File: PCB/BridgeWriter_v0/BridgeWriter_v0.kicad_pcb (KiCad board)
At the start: 4 copper layers, 100 x 60 mm, 195 parts, among them J1 USB_B, J10 Conn_01x04, J17 Conn_01x01, J18 Conn_01x01, J2 RJ45_Bel_SI-60062-F, J24 Conn_01x04, J25 Conn_01x04, J3 Conn_01x05, J4 Conn_01x06, J6 Conn_01x04, J7 Conn_01x04, J9 Micro_SD_Card_Det2, SW1 SW_Push, SW10 SW_Push, SW2 BOOT_MODE0, SW3 SW_Push, SW4 SW_Push, SW5 SW_Push, SW6 SW_Push, SW7 SW_Push, SW8 BOOT_MODE1, SW9 SW_Push, U1 STM32H723VGTx, U10 ADP3338AKCZ-3.3, U11 OKL-T/6-W12N-C, U2 W6300, U3 ESP32-C5-WROOM-1, U5 MCP2562-E-SN, U6 MCP2562-E-SN, U7 USB3343, U8 ADP3338AKCZ-3.3, U9 CH213K, Y1 FC2012SN 32.768K-70NNA0KC0, Y2 XRCGB25M000FFS1AR0, Y3 ECS-600-8-36B-CTN-TR

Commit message: change
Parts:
- removed C25, C26: 0.1uF, Capacitor_SMD:C_0603_1608Metric_Pad1.08x0.95mm_HandSolder
- removed J10: Conn_01x04, Connector_PinSocket_2.54mm:PinSocket_1x04_P2.54mm_Vertical
- added U12: PT86-091940LMR, My_Library:PT86-091940LMR, F.Cu at (189.6, 77.7)
- added U4: TLP293, Package_SO:SOIC-4_4.55x2.6mm_P1.27mm, B.Cu at (208.2, 127.0)
- C10, C3, C35, C49, C6, C61, R19, R20, R21, R22, R23, R25, R47, U6: moved to B.Cu
- R55: value 80k -> 10k; moved to B.Cu
- R56: value 10k -> 1k; moved to B.Cu
- moved C35 126.6 mm to (230.7, 92.1)
- moved C61 121.9 mm to (226.9, 92.2)
- moved R25 117.3 mm to (230.7, 90.7), turned to 180 degrees
- moved SW8 112.2 mm to (186.3, 124.2), turned to 90 degrees
- moved SW2 105.5 mm to (177.9, 124.3), turned to 90 degrees
- moved R47 105.4 mm to (226.9, 90.7), turned to 180 degrees
- moved R55 95.7 mm to (213.2, 127.3), turned to 90 degrees
- moved R56 85.0 mm to (202.2, 128.7), turned to 180 degrees
- moved R2 79.9 mm to (182.0, 120.9)
- moved C31 60.3 mm to (201.0, 109.2), turned to 180 degrees
- moved C51 55.6 mm to (188.1, 106.3), turned to -135 degrees
- moved C33 55.0 mm to (187.2, 104.5), turned to -90 degrees
- moved R23 53.5 mm to (142.4, 122.1), turned to 90 degrees
- moved C34 53.3 mm to (201.0, 108.0), turned to 180 degrees
- moved R19 51.6 mm to (154.4, 122.1), turned to 90 degrees
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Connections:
- J3 pad 2: SWDIO -> SWCLK
- J3 pad 3: SWCLK -> SWDIO
- J3 pad 4: +3.3V -> GND
- J3 pad 5: GND -> +3.3V
- R55 pad 2: POWER_MONITOR -> Net-(R55-Pad2)
- R56 pad 1: POWER_MONITOR -> Net-(R56-Pad1)
- R56 pad 2: GND -> +3.3V
- U1 pad 68: LPUART_TXD -> unconnected-(U1-PA9-Pad68)
- U1 pad 69: LPUART_RXD -> unconnected-(U1-PA10-Pad69)
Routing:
- net NRST: track 0.00 -> 43.7 mm, vias 0 -> 2
- net +3.3V: track 55.5 -> 83.4 mm, vias 7 -> 9
- net ESP_3.3V: track 16.7 -> 27.0 mm, vias 0 -> 1
- net SWDIO: track 0.00 -> 9.88 mm
- net SWCLK: track 0.00 -> 9.40 mm
- net Net-(R56-Pad1): track 0.00 -> 6.59 mm
- net Net-(C30-Pad1): track 0.00 -> 3.10 mm
- net Net-(C31-Pad1): track 0.00 -> 2.95 mm
- net Net-(R55-Pad2): track 0.00 -> 1.78 mm
- net ESP32_EN: track 0.00 -> 1.46 mm, vias 0 -> 1
- net ESP32_IO0: track 0.00 -> 1.45 mm, vias 0 -> 1
- net Wi-Fi_RESET: track 0.00 -> 0.66 mm, vias 0 -> 1
- net USB_RESET: track 0.00 -> 0.66 mm, vias 0 -> 1
- net FDCAN2_RESET: track 0.00 -> 0.66 mm, vias 0 -> 1
- net FDCAN1_RESET: track 0.00 -> 0.66 mm, vias 0 -> 1
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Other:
- board text added: "Ethernet"
- board text added: "FDCAN1"
- board text added: "FDCAN2"
- board text added: "GND"
- board text added: "MAX 14V"
- board text added: "RESET"
- board text added: "USB"
- board text added: "VCC"
- board text added: "Wi-Fi"

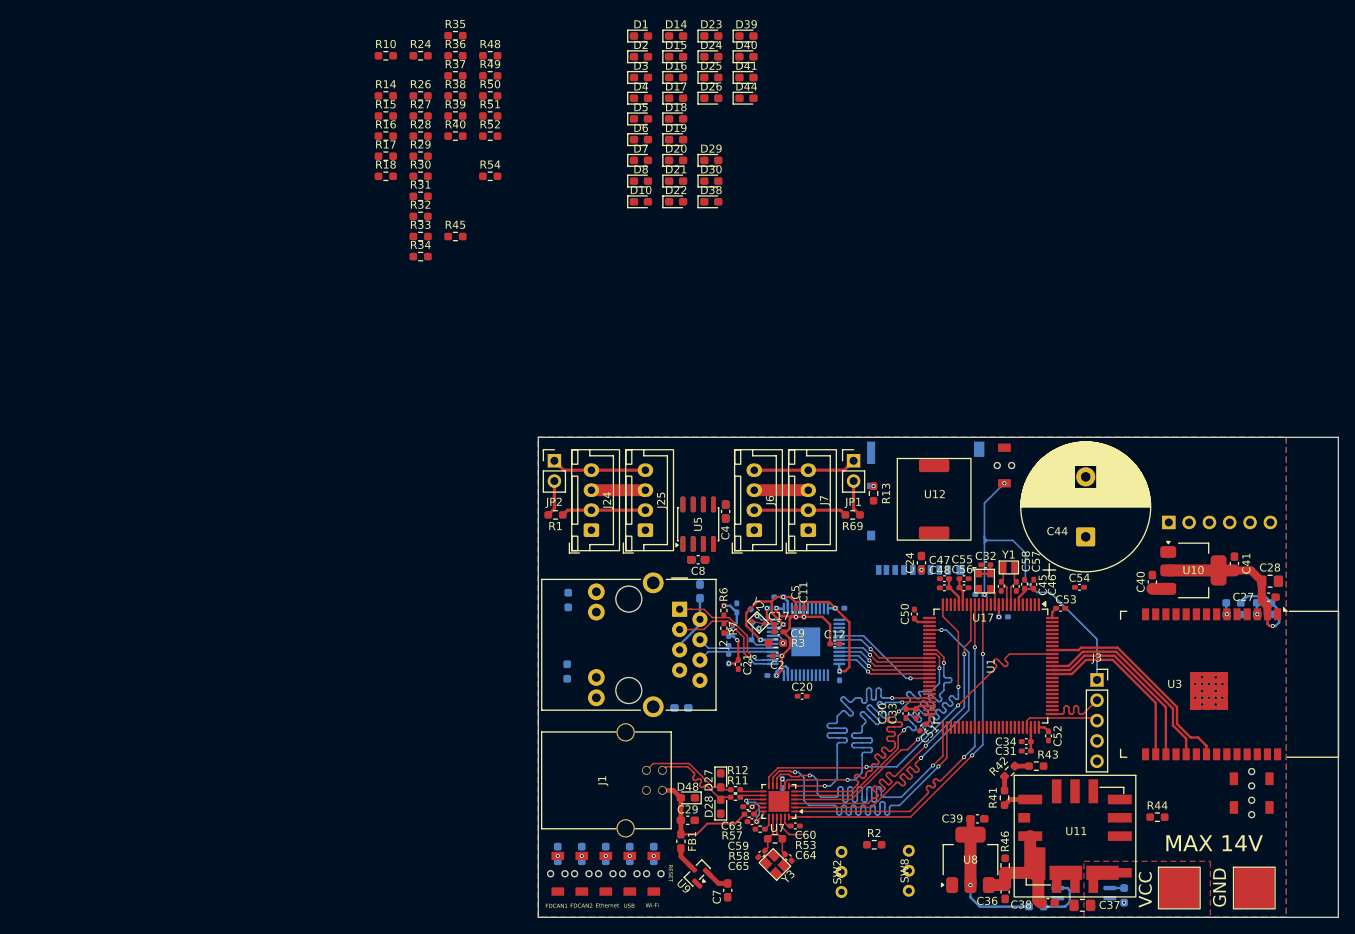
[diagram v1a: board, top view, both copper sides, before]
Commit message: All the wiring except the power is probably done.
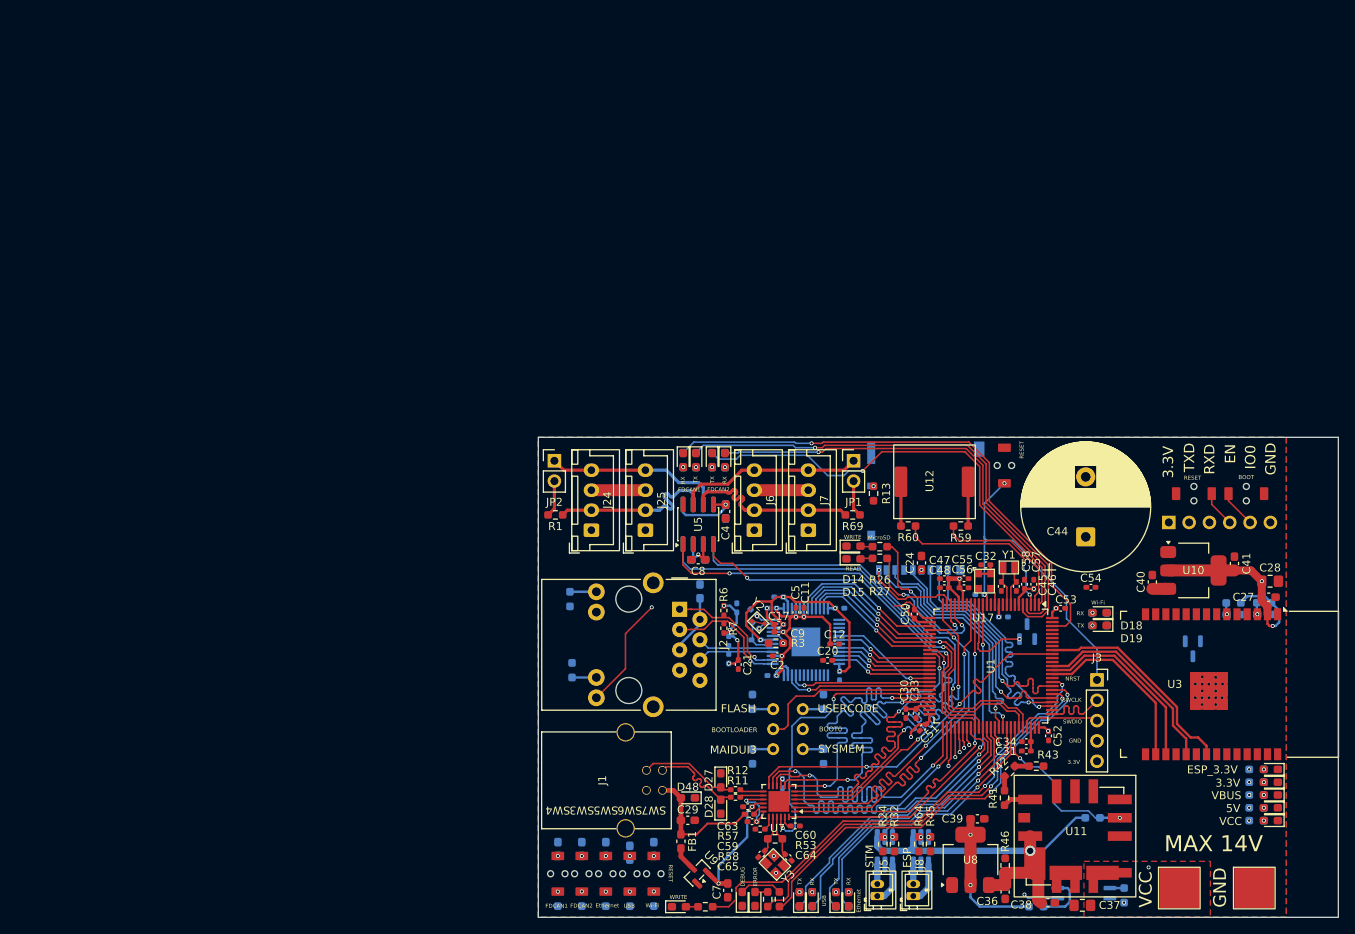
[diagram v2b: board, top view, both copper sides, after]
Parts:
- removed C1: 1uF, Capacitor_SMD:C_0603_1608Metric_Pad1.08x0.95mm_HandSolder
- removed D16, D38, D39: O, LED_SMD:LED_0603_1608Metric_Pad1.05x0.95mm_HandSolder
- removed D17, D20, D7: G, LED_SMD:LED_0603_1608Metric_Pad1.05x0.95mm_HandSolder
- removed D4, D8: W, LED_SMD:LED_0603_1608Metric_Pad1.05x0.95mm_HandSolder
- removed D44: LED, LED_SMD:LED_0603_1608Metric_Pad1.05x0.95mm_HandSolder
- removed R16, R28, R29, R48, R49, R52: 1k, Resistor_SMD:R_0603_1608Metric_Pad0.98x0.95mm_HandSolder
- added C25: 0.1uF, Capacitor_SMD:C_0603_1608Metric_Pad1.08x0.95mm_HandSolder, B.Cu at (154.4, 121.5)
- added C26: 0.1uF, Capacitor_SMD:C_0603_1608Metric_Pad1.08x0.95mm_HandSolder, B.Cu at (151.4, 121.9)
- added C66: 0.1uF, Capacitor_SMD:C_0603_1608Metric_Pad1.08x0.95mm_HandSolder, B.Cu at (142.4, 121.5)
- added C67: 0.1uF, Capacitor_SMD:C_0603_1608Metric_Pad1.08x0.95mm_HandSolder, B.Cu at (145.4, 121.5)
- added C68: 0.1uF, Capacitor_SMD:C_0603_1608Metric_Pad1.08x0.95mm_HandSolder, B.Cu at (148.4, 121.5)
- added J5: Conn_01x02, Connector_JST:JST_ZH_B2B-ZR_1x02_P1.50mm_Vertical, F.Cu at (182.4, 127.3)
- added J8: Conn_01x02, Connector_JST:JST_ZH_B2B-ZR_1x02_P1.50mm_Vertical, F.Cu at (186.9, 127.3)
- added R59: 330, Resistor_SMD:R_0603_1608Metric_Pad0.98x0.95mm_HandSolder, F.Cu at (192.8, 81.1)
- added R60: 330, Resistor_SMD:R_0603_1608Metric_Pad0.98x0.95mm_HandSolder, F.Cu at (186.2, 81.1)
- added R61: 1k, Resistor_SMD:R_0603_1608Metric_Pad0.98x0.95mm_HandSolder, B.Cu at (154.4, 127.7)
- added R62: 1k, Resistor_SMD:R_0603_1608Metric_Pad0.98x0.95mm_HandSolder, B.Cu at (166.8, 109.9)
- added R63: 10k, Resistor_SMD:R_0603_1608Metric_Pad0.98x0.95mm_HandSolder, B.Cu at (166.8, 103.1)
- added R64: 1k, Resistor_SMD:R_0603_1608Metric_Pad0.98x0.95mm_HandSolder, F.Cu at (187.6, 120.8)
- added U13: AM8068, Package_TO_SOT_SMD:TSOT-23-6_HandSoldering, B.Cu at (183.3, 121.7)
- added U14: AM8068, Package_TO_SOT_SMD:TSOT-23-6_HandSoldering, B.Cu at (187.8, 121.7)
- added U15: MCP9700x-ETT, Package_TO_SOT_SMD:SOT-23, B.Cu at (221.8, 96.4)
- added U16: MCP9700x-ETT, Package_TO_SOT_SMD:SOT-23, B.Cu at (201.1, 94.3)
- D15, D19, D22, D24, D26, D30: value B -> G
- R10, R14, R15, R17, R2, R30, R31, R33, R34, R35, R36, R37, R38, R39, R40, R44, R54: moved to B.Cu
- moved R10 142.8 mm to (229.8, 114.7)
- moved R14 141.6 mm to (229.8, 117.9)
- moved R15 139.0 mm to (229.8, 116.3)
- moved R17 134.0 mm to (229.8, 113.1)
- moved D1 125.8 mm to (231.6, 117.9), turned to 180 degrees
- moved D2 122.5 mm to (231.6, 116.3), turned to 180 degrees
- moved R54 121.1 mm to (229.8, 111.5)
- moved D3 119.3 mm to (231.6, 114.7), turned to 180 degrees
- moved D5 114.3 mm to (231.6, 113.1), turned to 180 degrees
- moved R24 114.2 mm to (183.1, 120.9), turned to -90 degrees
- moved R39 108.8 mm to (177.2, 127.7), turned to 90 degrees
- moved R40 107.3 mm to (178.8, 127.7), turned to 90 degrees
- moved R50 106.7 mm to (170.1, 127.7), turned to 90 degrees
- moved D10 106.0 mm to (231.6, 111.5), turned to 180 degrees
- moved D40 105.3 mm to (165.5, 127.7), turned to 90 degrees
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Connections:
- J2 pad SH: Net-(C1-Pad1) -> unconnected-(J2-PadSH)_1
- R19 pad 1: Wi-Fi_RESET -> +3.3V
- R19 pad 2: GND -> Net-(R19-Pad2)
- R20 pad 1: USB_RESET -> +3.3V
- R20 pad 2: GND -> Net-(R20-Pad2)
- R21 pad 1: Ethernet_RESET -> +3.3V
- R21 pad 2: GND -> Net-(R21-Pad2)
- R22 pad 1: FDCAN2_RESET -> +3.3V
- R22 pad 2: GND -> Net-(R22-Pad2)
- R23 pad 1: FDCAN1_RESET -> +3.3V
- R23 pad 2: GND -> Net-(SW2-A)
- R24 pad 1: Ethernet_Active -> FAN_INB_STM
- R24 pad 2: Net-(D7-A) -> GND
- R32 pad 1: USB_Active -> FAN_INA_STM
- R32 pad 2: Net-(D20-A) -> GND
- R45 pad 1: PGOOD -> FAN_INA_ESP
- R45 pad 2: Net-(D8-A) -> GND
- SW2 pad 1: +3.3V -> Net-(SW2-A)
- SW3 pad 1: +3.3V -> Net-(R22-Pad2)
- SW4 pad 1: +3.3V -> Net-(R21-Pad2)
- SW5 pad 1: +3.3V -> Net-(R20-Pad2)
- SW6 pad 1: +3.3V -> Net-(R19-Pad2)
- SW7 pad 1: +3.3V -> Net-(R61-Pad2)
- SW8 pad 1: RAM_BOOTLOADER -> Net-(SW8-A)
- SW8 pad 2: +3.3V -> BOOTMODE
- SW8 pad 3: FLASH_USERCODE -> Net-(SW8-C)
- U1 pad 1: unconnected-(U1-PE2-Pad1) -> FDCAN2_RX
- U1 pad 16: unconnected-(U1-PC1-Pad16) -> Th_STM
- U1 pad 2: unconnected-(U1-PE3-Pad2) -> Speaker_In2
- U1 pad 22: unconnected-(U1-PA0-Pad22) -> SDMMC_READ
- U1 pad 23: unconnected-(U1-PA1-Pad23) -> SDMMC_WRITE
- U1 pad 24: unconnected-(U1-PA2-Pad24) -> SDMMC_CHECK
- U1 pad 28: unconnected-(U1-PA4-Pad28) -> W6300_LNK
- U1 pad 3: unconnected-(U1-PE4-Pad3) -> Speaker_In1
- U1 pad 30: unconnected-(U1-PA6-Pad30) -> W6300_SPD
- U1 pad 31: unconnected-(U1-PA7-Pad31) -> W6300_DPX
- U1 pad 32: unconnected-(U1-PC4-Pad32) -> W6300_ACT
- U1 pad 33: unconnected-(U1-PC5-Pad33) -> W6300_COL
- U1 pad 4: unconnected-(U1-PE5-Pad4) -> FDCAN2_TX
- U1 pad 42: unconnected-(U1-PE12-Pad42) -> W6300_INT
- U1 pad 43: unconnected-(U1-PE13-Pad43) -> W6300_RST
- U1 pad 44: unconnected-(U1-PE14-Pad44) -> BOOTMODE
- U1 pad 45: unconnected-(U1-PE15-Pad45) -> USB3343_RESETB
- U1 pad 5: unconnected-(U1-PE6-Pad5) -> FDCAN1_TX
- U1 pad 53: unconnected-(U1-PB14-Pad53) -> Wi-Fi_RESET
- U1 pad 54: unconnected-(U1-PB15-Pad54) -> USB_RESET
- U1 pad 55: unconnected-(U1-PD8-Pad55) -> Ethernet_RESET
- U1 pad 56: unconnected-(U1-PD9-Pad56) -> FDCAN2_RESET
- U1 pad 57: unconnected-(U1-PD10-Pad57) -> FDCAN1_RESET
- U1 pad 58: unconnected-(U1-PD11-Pad58) -> USB_TX
- U1 pad 61: unconnected-(U1-PD14-Pad61) -> USB_RX
- U1 pad 62: unconnected-(U1-PD15-Pad62) -> Ethernet_TX
- U1 pad 63: unconnected-(U1-PC6-Pad63) -> Ethernet_RX
- U1 pad 64: unconnected-(U1-PC7-Pad64) -> POWER_MONITOR
- U1 pad 67: unconnected-(U1-PA8-Pad67) -> FAN_INB_STM
- U1 pad 68: unconnected-(U1-PA9-Pad68) -> FAN_INA_STM
- U1 pad 69: unconnected-(U1-PA10-Pad69) -> PGOOD
- U1 pad 81: unconnected-(U1-PD0-Pad81) -> ERROR_LED
- U1 pad 82: unconnected-(U1-PD1-Pad82) -> DEBUG_LED
- U1 pad 84: unconnected-(U1-PD3-Pad84) -> WRITER_MODE
- U1 pad 98: unconnected-(U1-PE1-Pad98) -> FDCAN1_RX
- U12 pad 1: unconnected-(U12-In-Pad1) -> Net-(R60-Pad2)
- U12 pad 2: unconnected-(U12-In-Pad2) -> Net-(R59-Pad2)
- U3 pad 7: unconnected-(U3-IO1-Pad7) -> Th_ESP
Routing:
- net VBUS: track 16.2 -> 112.4 mm, vias 0 -> 1
- net +5V: track 36.4 -> 116.2 mm, vias 1 -> 5
- net FDCAN1_RESET: track 0.66 -> 69.5 mm, vias 1 -> 2
- net FDCAN1_RX: track 0.00 -> 66.6 mm, vias 0 -> 1
- net FDCAN1_TX: track 0.00 -> 64.1 mm, vias 0 -> 1
- net W6300_LNK: track 0.00 -> 63.9 mm, vias 0 -> 2
- net FDCAN2_RESET: track 0.66 -> 62.5 mm, vias 1 -> 2
- net FDCAN_RXD_1: track 0.00 -> 59.8 mm, vias 0 -> 1
- net WRITER_MODE: track 0.00 -> 59.7 mm, vias 0 -> 2
- net FDCAN2_TX: track 0.00 -> 58.0 mm, vias 0 -> 1
- net Ethernet_RESET: track 0.66 -> 58.6 mm, vias 1 -> 2
- net FDCAN2_RX: track 0.00 -> 57.7 mm, vias 0 -> 1
- net W6300_ACT: track 0.00 -> 56.3 mm, vias 0 -> 1
- net FDCAN_TXD_1: track 0.00 -> 56.3 mm, vias 0 -> 1
- net USB_RESET: track 0.66 -> 55.2 mm, vias 1 -> 2
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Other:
- board text added: "3.3V"
- board text added: "5V"
- board text added: "BOOT"
- board text added: "BOOT0"
- board text added: "BOOTLOADER"
- board text added: "DEBUG"
- board text added: "EN"
- board text added: "ERROR"
- board text added: "ESP"
- board text added: "ESP_3.3V"
- board text added: "FLASH"
- board text added: "IO0"
- board text added: "MAIDUI3"
- board text added: "MicroSD"
- board text added: "NRST"
- board text added: "READ"
- board text added: "RX"
- board text added: "RXD"
- board text added: "STM"
- board text added: "SWCLK"
- board text added: "SWDIO"
- board text added: "SYSMEM"
- board text added: "TX"
- board text added: "TXD"
- board text added: "USERCODE"
- board text added: "VBUS"
- board text added: "WRITE"

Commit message: Completed PCB
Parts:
- moved C54 19.7 mm to (205.0, 108.0), turned to -90 degrees
- moved C20 6.24 mm to (179.7, 92.7), turned to 135 degrees
- moved U15 2.13 mm to (223.8, 95.8)
- moved U3 0.11 mm to (219.4, 100.8)
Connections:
- U3 pad 13: unconnected-(U3-IO13-Pad13) -> Wi-Fi_RX
- U3 pad 14: unconnected-(U3-IO14-Pad14) -> Wi-Fi_TX
- U3 pad 15: unconnected-(U3-IO28-Pad15) -> FAN_INB_ESP
- U3 pad 18: unconnected-(U3-IO27-Pad18) -> FAN_INA_ESP
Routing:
- net +3.3V: track 135.7 -> 426.2 mm, vias 18 -> 26
- net +5V: track 116.2 -> 292.2 mm, vias 5 -> 10
- net GND: track 14.1 -> 92.8 mm, vias 3 -> 183
- net STM32_BOOT0: track 0.00 -> 36.9 mm, vias 0 -> 1
- net FAN_INA_ESP: track 0.26 -> 36.2 mm, vias 1 -> 2
- net TXD0: track 0.00 -> 34.6 mm, vias 0 -> 1
- net RXD0: track 0.00 -> 33.9 mm, vias 0 -> 1
- net FAN_INB_ESP: track 0.27 -> 33.4 mm, vias 1 -> 2
- net Wi-Fi_RX: track 0.00 -> 6.86 mm, vias 0 -> 1
- net ESP_3.3V: track 51.6 -> 57.6 mm, vias 3 -> 4
- net Wi-Fi_TX: track 0.00 -> 5.72 mm, vias 0 -> 1
- net Th_ESP: track 0.00 -> 2.74 mm, vias 0 -> 1
- net +1V2: track 28.0 -> 29.1 mm, vias 6 -> 7
- net PGOOD: track 21.2 -> 21.0 mm, vias 2 -> 3
